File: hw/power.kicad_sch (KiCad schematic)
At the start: 46 parts, among them J9 Expansion, Q8 DMC2053UVT, U1 RT8096B, U2 RT8096B, U3 RT8096B, U5 TPS563249DDC

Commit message: finalizing...
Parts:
- removed C6: 6p8, Capacitor_SMD:C_0603_1608Metric, symbol Device:C_Small
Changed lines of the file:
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@@
   (junction (at 86.36 72.39) (diameter 0) (color 0 0 0 0)
   )
-  (junction (at 93.98 34.29) (diameter 0) (color 0 0 0 0)
-  )
   (junction (at 104.14 31.75) (diameter 0) (color 0 0 0 0)
   )
@@
   (junction (at 58.42 69.85) (diameter 0) (color 0 0 0 0)
   )
-  (junction (at 86.36 34.29) (diameter 0) (color 0 0 0 0)
-  )
   (junction (at 69.85 43.18) (diameter 0) (color 0 0 0 0)
   )
@@
     (stroke (width 0) (type default))
   )
-  (wire (pts (xy 87.63 38.1) (xy 86.36 38.1))
-    (stroke (width 0) (type default))
-  )
   (wire (pts (xy 115.57 138.43) (xy 119.38 138.43))
     (stroke (width 0) (type default))
@@
     (stroke (width 0) (type default))
   )
-  (wire (pts (xy 86.36 34.29) (xy 87.63 34.29))
-    (stroke (width 0) (type default))
-  )
   (wire (pts (xy 93.98 113.03) (xy 93.98 109.22))
     (stroke (width 0) (type default))
@@
     (stroke (width 0) (type default))
   )
-  (wire (pts (xy 81.28 34.29) (xy 86.36 34.29))
+  (wire (pts (xy 81.28 34.29) (xy 87.63 34.29))
     (stroke (width 0) (type default))
   )
@@
     (stroke (width 0) (type default))
   )
-  (wire (pts (xy 93.98 38.1) (xy 93.98 34.29))
-    (stroke (width 0) (type default))
-  )
   (wire (pts (xy 224.79 38.1) (xy 248.92 38.1))
     (stroke (width 0) (type default))
@@
     (stroke (width 0) (type default))
   )
-  (wire (pts (xy 86.36 38.1) (xy 86.36 34.29))
-    (stroke (width 0) (type default))
-  )
   (wire (pts (xy 58.42 132.08) (xy 77.47 132.08))
     (stroke (width 0) (type default))
@@
     (stroke (width 0) (type default))
   )
-  (wire (pts (xy 92.71 38.1) (xy 93.98 38.1))
-    (stroke (width 0) (type default))
-  )
   (wire (pts (xy 60.96 57.15) (xy 58.42 57.15))
     (stroke (width 0) (type default))
@@
     (stroke (width 0) (type default))
   )
-  (wire (pts (xy 93.98 34.29) (xy 99.06 34.29))
-    (stroke (width 0) (type default))
-  )
   (wire (pts (xy 241.3 58.42) (xy 252.73 58.42))
     (stroke (width 0) (type default))
@@
     (stroke (width 0) (type default))
   )
-  (wire (pts (xy 92.71 34.29) (xy 93.98 34.29))
+  (wire (pts (xy 92.71 34.29) (xy 99.06 34.29))
     (stroke (width 0) (type default))
   )
@@
         (path "/7c8a1f8d-8834-4c9b-aaae-1f231e9b09a1/00000000-0000-0000-0000-00006086f2e3"
           (reference "C5") (unit 1)
-        )
-      )
-    )
-  )
-  (symbol (lib_id "Device:C_Small") (at 90.17 38.1 270) (unit 1)
-    (in_bom yes) (on_board yes) (dnp no)
-    (property "Reference" "C6" (at 93.98 40.64 90)
-      (effects (font (size 1.27 1.27)))
-    )
-    (property "Value" "6p8" (at 90.17 41.91 90)
-      (effects (font (size 1.27 1.27)))
-    )
-    (property "Footprint" "Capacitor_SMD:C_0603_1608Metric" (at 90.17 38.1 0)
-      (effects (font (size 1.27 1.27)) hide)
-    )
-    (property "Datasheet" "~" (at 90.17 38.1 0)
-      (effects (font (size 1.27 1.27)) hide)
-    )
-    (property "Part" "885012006050" (at 90.17 38.1 90)
-      (effects (font (size 1.27 1.27)) hide)
-    )
-    (property "Manufacturer" "Wurth" (at 90.17 38.1 90)
-      (effects (font (size 1.27 1.27)) hide)
-    )
-    (pin "1")
-    (pin "2")
-    (instances
-      (project "usbadc"
-        (path "/7c8a1f8d-8834-4c9b-aaae-1f231e9b09a1/00000000-0000-0000-0000-00006086f2e3"
-          (reference "C6") (unit 1)
         )
       )
@@
     )
   )
-  (symbol (lib_id "Transistor_FET:DMC2053UVT") (at 220.98 58.42 270) (mirror x) (unit 2)
+  (symbol (lib_name "DMC2053UVT_1") (lib_id "Transistor_FET:DMC2053UVT") (at 220.98 58.42 270) (mirror x) (unit 2)
     (in_bom yes) (on_board yes) (dnp no)
     (property "Reference" "Q8" (at 221.6237 55.753 0)

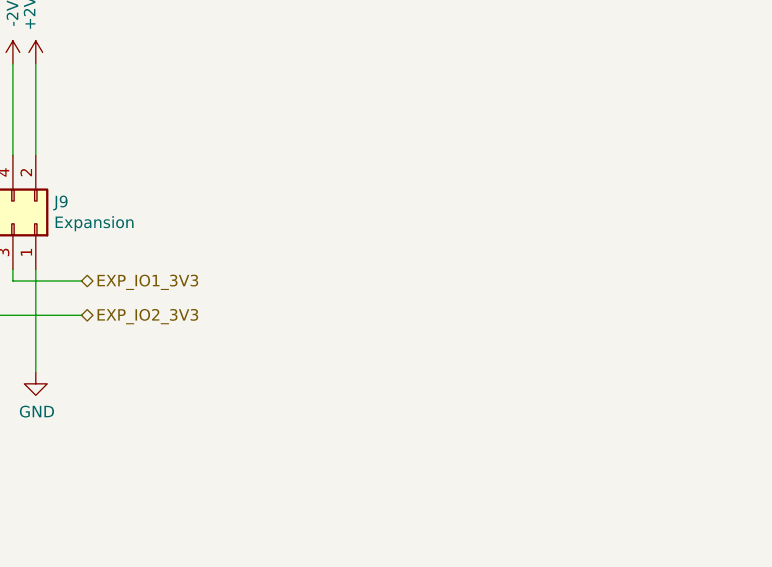
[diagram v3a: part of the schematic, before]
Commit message: PCB: added a few ground/test-points
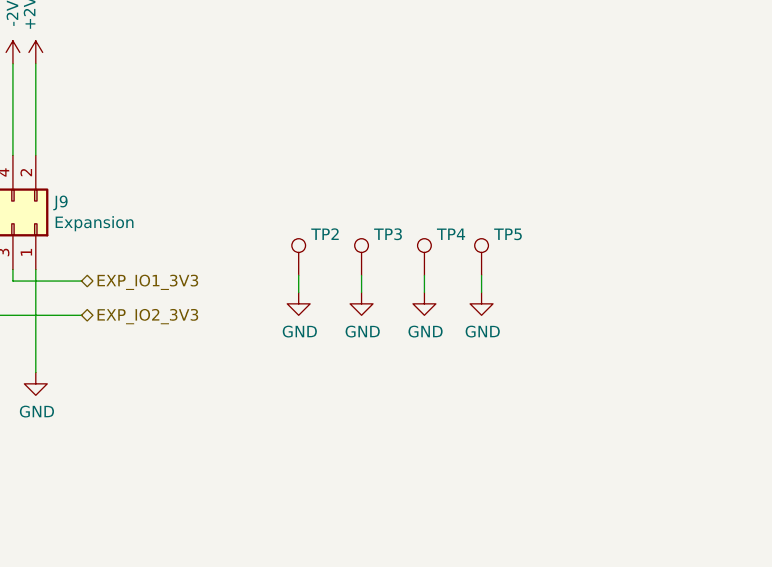
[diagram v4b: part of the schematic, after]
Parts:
- added TP2, TP3, TP4, TP5: TestPoint, Connector_PinHeader_2.54mm:PinHeader_1x01_P2.54mm_Vertical, symbol Connector:TestPoint
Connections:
- net GND: now also TP2.1, TP3.1, TP4.1, TP5.1
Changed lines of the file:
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@@
+    (stroke (width 0) (type default))
+  )
+  (wire (pts (xy 232.41 142.875) (xy 232.41 144.78))
     (stroke (width 0) (type default))
   )
@@
     (stroke (width 0) (type default))
   )
+  (wire (pts (xy 225.425 142.875) (xy 225.425 144.78))
+    (stroke (width 0) (type default))
+  )
   (wire (pts (xy 226.06 58.42) (xy 229.87 58.42))
     (stroke (width 0) (type default))
@@
     (stroke (width 0) (type default))
   )
+  (wire (pts (xy 238.76 142.875) (xy 238.76 144.78))
+    (stroke (width 0) (type default))
+  )
   (wire (pts (xy 189.23 129.54) (xy 189.23 119.38))
     (stroke (width 0) (type default))
@@
   )
   (wire (pts (xy 86.36 113.03) (xy 86.36 109.22))
+    (stroke (width 0) (type default))
+  )
+  (wire (pts (xy 218.44 142.875) (xy 218.44 144.78))
     (stroke (width 0) (type default))
   )
@@
     )
   )
+  (symbol (lib_id "power:GND") (at 238.76 144.78 0) (unit 1)
+    (in_bom yes) (on_board yes) (dnp no)
+    (property "Reference" "#PWR0122" (at 238.76 151.13 0)
+      (effects (font (size 1.27 1.27)) hide)
+    )
+    (property "Value" "GND" (at 238.887 149.1742 0)
+      (effects (font (size 1.27 1.27)))
+    )
+    (property "Footprint" "" (at 238.76 144.78 0)
+      (effects (font (size 1.27 1.27)) hide)
+    )
+    (property "Datasheet" "" (at 238.76 144.78 0)
+      (effects (font (size 1.27 1.27)) hide)
+    )
+    (pin "1")
+    (instances
+      (project "usbadc"
+        (path "/7c8a1f8d-8834-4c9b-aaae-1f231e9b09a1/00000000-0000-0000-0000-00006086f2e3"
+          (reference "#PWR0122") (unit 1)
+        )
+      )
+    )
+  )
   (symbol (lib_id "power:GNDA") (at 139.7 139.7 0) (unit 1)
     (in_bom yes) (on_board yes) (dnp no)
@@
     )
   )
+  (symbol (lib_id "Connector:TestPoint") (at 218.44 142.875 0) (unit 1)
+    (in_bom yes) (on_board yes) (dnp no) (fields_autoplaced)
+    (property "Reference" "TP2" (at 219.837 138.3609 0)
+      (effects (font (size 1.27 1.27)) (justify left))
+    )
+    (property "Value" "TestPoint" (at 219.837 140.7851 0)
+      (effects (font (size 1.27 1.27)) (justify left) hide)
+    )
+    (property "Footprint" "Connector_PinHeader_2.54mm:PinHeader_1x01_P2.54mm_Vertical" (at 223.52 142.875 0)
+      (effects (font (size 1.27 1.27)) hide)
+    )
+    (property "Datasheet" "~" (at 223.52 142.875 0)
+      (effects (font (size 1.27 1.27)) hide)
+    )
+    (pin "1")
+    (instances
+      (project "usbadc"
+        (path "/7c8a1f8d-8834-4c9b-aaae-1f231e9b09a1/00000000-0000-0000-0000-00006086f2e3"
+          (reference "TP2") (unit 1)
+        )
+      )
+    )
+  )
   (symbol (lib_id "power:PWR_FLAG") (at 102.87 153.67 0) (unit 1)
     (in_bom yes) (on_board yes) (dnp no)
@@
     )
   )
+  (symbol (lib_id "power:GND") (at 218.44 144.78 0) (unit 1)
+    (in_bom yes) (on_board yes) (dnp no)
+    (property "Reference" "#PWR0112" (at 218.44 151.13 0)
+      (effects (font (size 1.27 1.27)) hide)
+    )
+    (property "Value" "GND" (at 218.567 149.1742 0)
+      (effects (font (size 1.27 1.27)))
+    )
+    (property "Footprint" "" (at 218.44 144.78 0)
+      (effects (font (size 1.27 1.27)) hide)
+    )
+    (property "Datasheet" "" (at 218.44 144.78 0)
+      (effects (font (size 1.27 1.27)) hide)
+    )
+    (pin "1")
+    (instances
+      (project "usbadc"
+        (path "/7c8a1f8d-8834-4c9b-aaae-1f231e9b09a1/00000000-0000-0000-0000-00006086f2e3"
+          (reference "#PWR0112") (unit 1)
+        )
+      )
+    )
+  )
   (symbol (lib_id "fmc:-2V5_analog") (at 186.69 119.38 0) (unit 1)
     (in_bom yes) (on_board yes) (dnp no)
@@
     )
   )
+  (symbol (lib_id "Connector:TestPoint") (at 238.76 142.875 0) (unit 1)
+    (in_bom yes) (on_board yes) (dnp no) (fields_autoplaced)
+    (property "Reference" "TP5" (at 240.157 138.3609 0)
+      (effects (font (size 1.27 1.27)) (justify left))
+    )
+    (property "Value" "TestPoint" (at 240.157 140.7851 0)
+      (effects (font (size 1.27 1.27)) (justify left) hide)
+    )
+    (property "Footprint" "Connector_PinHeader_2.54mm:PinHeader_1x01_P2.54mm_Vertical" (at 243.84 142.875 0)
+      (effects (font (size 1.27 1.27)) hide)
+    )
+    (property "Datasheet" "~" (at 243.84 142.875 0)
+      (effects (font (size 1.27 1.27)) hide)
+    )
+    (pin "1")
+    (instances
+      (project "usbadc"
+        (path "/7c8a1f8d-8834-4c9b-aaae-1f231e9b09a1/00000000-0000-0000-0000-00006086f2e3"
+          (reference "TP5") (unit 1)
+        )
+      )
+    )
+  )
   (symbol (lib_id "Device:C_Small") (at 57.15 140.97 180) (unit 1)
     (in_bom yes) (on_board yes) (dnp no)
@@
     )
   )
+  (symbol (lib_id "Connector:TestPoint") (at 225.425 142.875 0) (unit 1)
+    (in_bom yes) (on_board yes) (dnp no) (fields_autoplaced)
+    (property "Reference" "TP3" (at 226.822 138.3609 0)
+      (effects (font (size 1.27 1.27)) (justify left))
+    )
+    (property "Value" "TestPoint" (at 226.822 140.7851 0)
+      (effects (font (size 1.27 1.27)) (justify left) hide)
+    )
+    (property "Footprint" "Connector_PinHeader_2.54mm:PinHeader_1x01_P2.54mm_Vertical" (at 230.505 142.875 0)
+      (effects (font (size 1.27 1.27)) hide)
+    )
+    (property "Datasheet" "~" (at 230.505 142.875 0)
+      (effects (font (size 1.27 1.27)) hide)
+    )
+    (pin "1")
+    (instances
+      (project "usbadc"
+        (path "/7c8a1f8d-8834-4c9b-aaae-1f231e9b09a1/00000000-0000-0000-0000-00006086f2e3"
+          (reference "TP3") (unit 1)
+        )
+      )
+    )
+  )
   (symbol (lib_id "fmc:+2V5_analog") (at 252.73 88.9 0) (mirror y) (unit 1)
     (in_bom yes) (on_board yes) (dnp no)
@@
         (path "/7c8a1f8d-8834-4c9b-aaae-1f231e9b09a1/00000000-0000-0000-0000-00006086f2e3"
           (reference "L2") (unit 1)
+        )
+      )
+    )
+  )
+  (symbol (lib_id "power:GND") (at 232.41 144.78 0) (unit 1)
+    (in_bom yes) (on_board yes) (dnp no)
+    (property "Reference" "#PWR0121" (at 232.41 151.13 0)
+      (effects (font (size 1.27 1.27)) hide)
+    )
+    (property "Value" "GND" (at 232.537 149.1742 0)
+      (effects (font (size 1.27 1.27)))
+    )
+    (property "Footprint" "" (at 232.41 144.78 0)
+      (effects (font (size 1.27 1.27)) hide)
+    )
+    (property "Datasheet" "" (at 232.41 144.78 0)
+      (effects (font (size 1.27 1.27)) hide)
+    )
+    (pin "1")
+    (instances
+      (project "usbadc"
+        (path "/7c8a1f8d-8834-4c9b-aaae-1f231e9b09a1/00000000-0000-0000-0000-00006086f2e3"
+          (reference "#PWR0121") (unit 1)
         )
       )
@@
     )
   )
+  (symbol (lib_id "power:GND") (at 225.425 144.78 0) (unit 1)
+    (in_bom yes) (on_board yes) (dnp no)
+    (property "Reference" "#PWR0115" (at 225.425 151.13 0)
+      (effects (font (size 1.27 1.27)) hide)
+    )
+    (property "Value" "GND" (at 225.552 149.1742 0)
+      (effects (font (size 1.27 1.27)))
+    )
+    (property "Footprint" "" (at 225.425 144.78 0)
+      (effects (font (size 1.27 1.27)) hide)
+    )
+    (property "Datasheet" "" (at 225.425 144.78 0)
+      (effects (font (size 1.27 1.27)) hide)
+    )
+    (pin "1")
+    (instances
+      (project "usbadc"
+        (path "/7c8a1f8d-8834-4c9b-aaae-1f231e9b09a1/00000000-0000-0000-0000-00006086f2e3"
+          (reference "#PWR0115") (unit 1)
+        )
+      )
+    )
+  )
   (symbol (lib_id "power:+1V2") (at 124.46 31.75 0) (unit 1)
     (in_bom yes) (on_board yes) (dnp no) (fields_autoplaced)
@@
         )
       )
+    )
+  )
+  (symbol (lib_id "Connector:TestPoint") (at 232.41 142.875 0) (unit 1)
+    (in_bom yes) (on_board yes) (dnp no) (fields_autoplaced)
+    (property "Reference" "TP4" (at 233.807 138.3609 0)
+      (effects (font (size 1.27 1.27)) (justify left))
+    )
+    (property "Value" "TestPoint" (at 233.807 140.7851 0)
+      (effects (font (size 1.27 1.27)) (justify left) hide)
+    )
+    (property "Footprint" "Connector_PinHeader_2.54mm:PinHeader_1x01_P2.54mm_Vertical" (at 237.49 142.875 0)
+      (effects (font (size 1.27 1.27)) hide)
+    )
+    (property "Datasheet" "~" (at 237.49 142.875 0)
+      (effects (font (size 1.27 1.27)) hide)
+    )
+    (pin "1")
+    (instances
+      (project "usbadc"
+        (path "/7c8a1f8d-8834-4c9b-aaae-1f231e9b09a1/00000000-0000-0000-0000-00006086f2e3"
+          (reference "TP4") (unit 1)
+        )
+      )

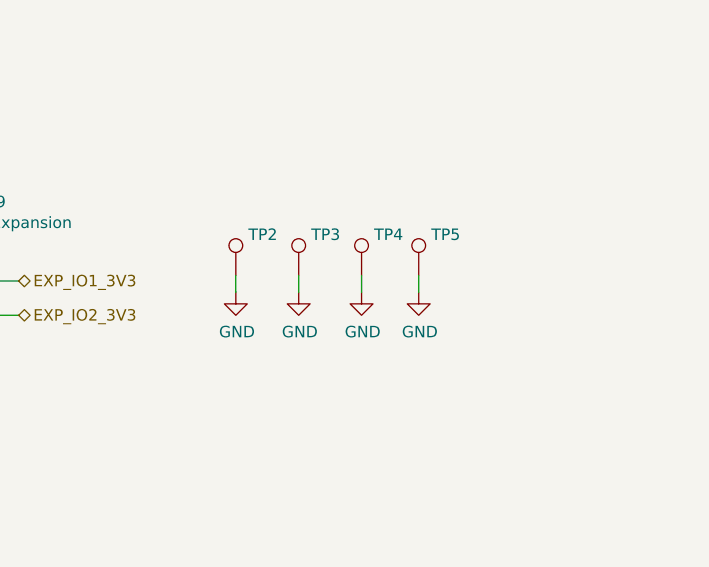
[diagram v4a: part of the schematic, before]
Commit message: PCB: cleaned up test points
(some use too much real-estate on inner Vcc layer)
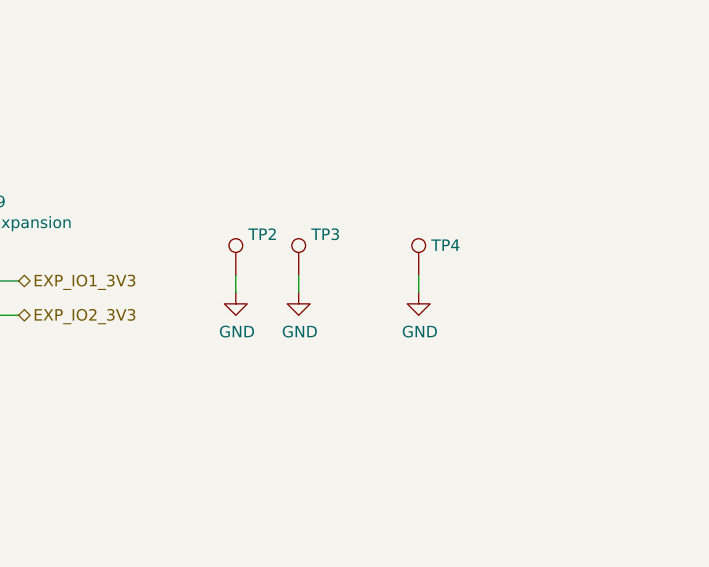
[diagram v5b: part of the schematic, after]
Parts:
- removed TP4: TestPoint, Connector_PinHeader_2.54mm:PinHeader_1x01_P2.54mm_Vertical, symbol Connector:TestPoint
- renumbered TP5 to TP4
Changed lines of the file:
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@@
-    (stroke (width 0) (type default))
-  )
-  (wire (pts (xy 232.41 142.875) (xy 232.41 144.78))
     (stroke (width 0) (type default))
   )
@@
   (symbol (lib_id "Connector:TestPoint") (at 238.76 142.875 0) (unit 1)
     (in_bom yes) (on_board yes) (dnp no) (fields_autoplaced)
-    (property "Reference" "TP5" (at 240.157 138.3609 0)
+    (property "Reference" "TP4" (at 240.157 139.573 0)
       (effects (font (size 1.27 1.27)) (justify left))
     )
@@
       (project "usbadc"
         (path "/7c8a1f8d-8834-4c9b-aaae-1f231e9b09a1/00000000-0000-0000-0000-00006086f2e3"
-          (reference "TP5") (unit 1)
+          (reference "TP4") (unit 1)
         )
       )
@@
     )
   )
-  (symbol (lib_id "power:GND") (at 232.41 144.78 0) (unit 1)
-    (in_bom yes) (on_board yes) (dnp no)
-    (property "Reference" "#PWR0121" (at 232.41 151.13 0)
-      (effects (font (size 1.27 1.27)) hide)
-    )
-    (property "Value" "GND" (at 232.537 149.1742 0)
-      (effects (font (size 1.27 1.27)))
-    )
-    (property "Footprint" "" (at 232.41 144.78 0)
-      (effects (font (size 1.27 1.27)) hide)
-    )
-    (property "Datasheet" "" (at 232.41 144.78 0)
-      (effects (font (size 1.27 1.27)) hide)
-    )
-    (pin "1")
-    (instances
-      (project "usbadc"
-        (path "/7c8a1f8d-8834-4c9b-aaae-1f231e9b09a1/00000000-0000-0000-0000-00006086f2e3"
-          (reference "#PWR0121") (unit 1)
-        )
-      )
-    )
-  )
   (symbol (lib_id "Device:R_Small") (at 58.42 127 180) (unit 1)
     (in_bom yes) (on_board yes) (dnp no)
@@
         )
       )
-    )
-  )
-  (symbol (lib_id "Connector:TestPoint") (at 232.41 142.875 0) (unit 1)
-    (in_bom yes) (on_board yes) (dnp no) (fields_autoplaced)
-    (property "Reference" "TP4" (at 233.807 138.3609 0)
-      (effects (font (size 1.27 1.27)) (justify left))
-    )
-    (property "Value" "TestPoint" (at 233.807 140.7851 0)
-      (effects (font (size 1.27 1.27)) (justify left) hide)
-    )
-    (property "Footprint" "Connector_PinHeader_2.54mm:PinHeader_1x01_P2.54mm_Vertical" (at 237.49 142.875 0)
-      (effects (font (size 1.27 1.27)) hide)
-    )
-    (property "Datasheet" "~" (at 237.49 142.875 0)
-      (effects (font (size 1.27 1.27)) hide)
-    )
-    (pin "1")
-    (instances
-      (project "usbadc"
-        (path "/7c8a1f8d-8834-4c9b-aaae-1f231e9b09a1/00000000-0000-0000-0000-00006086f2e3"
-          (reference "TP4") (unit 1)
-        )
-      )

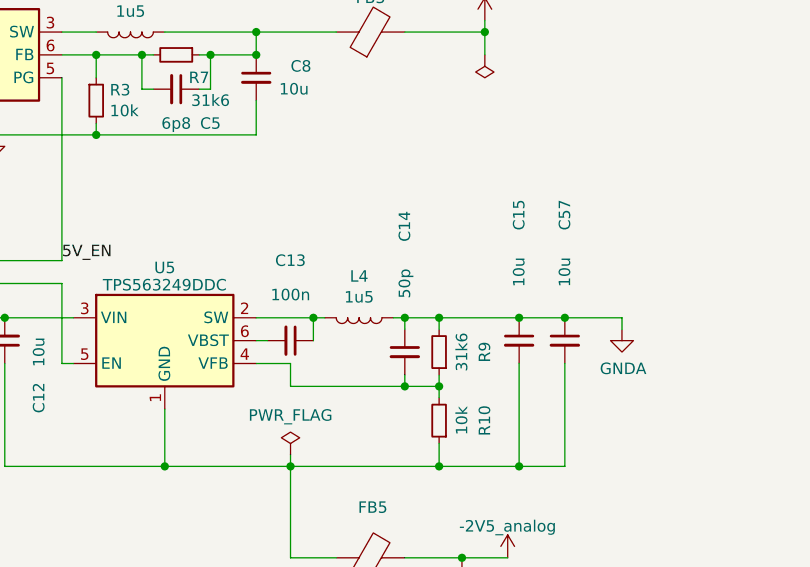
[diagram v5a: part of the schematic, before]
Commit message: updated some component values
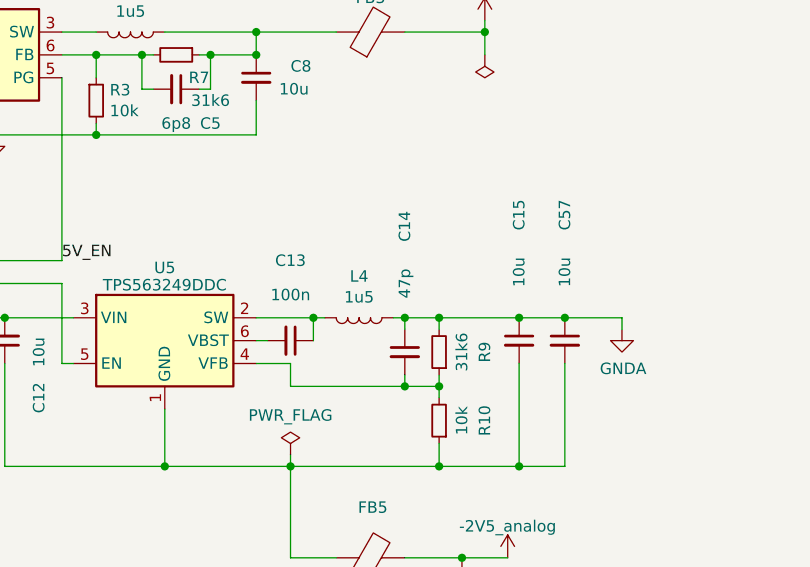
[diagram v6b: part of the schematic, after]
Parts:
- C14: value 50p -> 47p
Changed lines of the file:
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@@
       (effects (font (size 1.27 1.27)))
     )
-    (property "Value" "50p" (at 115.57 134.62 90)
+    (property "Value" "47p" (at 115.57 134.62 90)
       (effects (font (size 1.27 1.27)))
     )
